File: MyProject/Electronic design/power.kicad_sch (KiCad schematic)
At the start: 7 parts

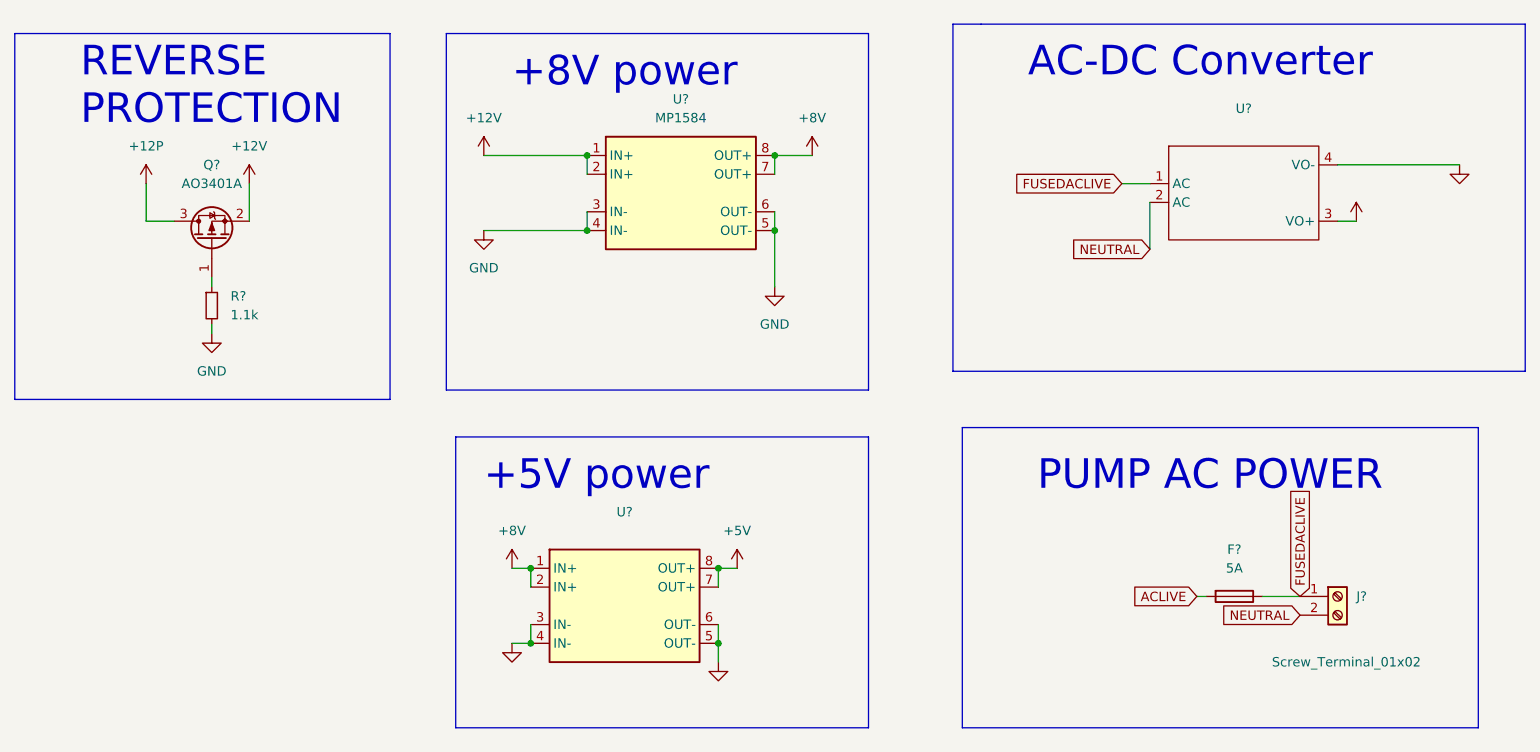
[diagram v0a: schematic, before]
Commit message: Shortening file names for Windows users
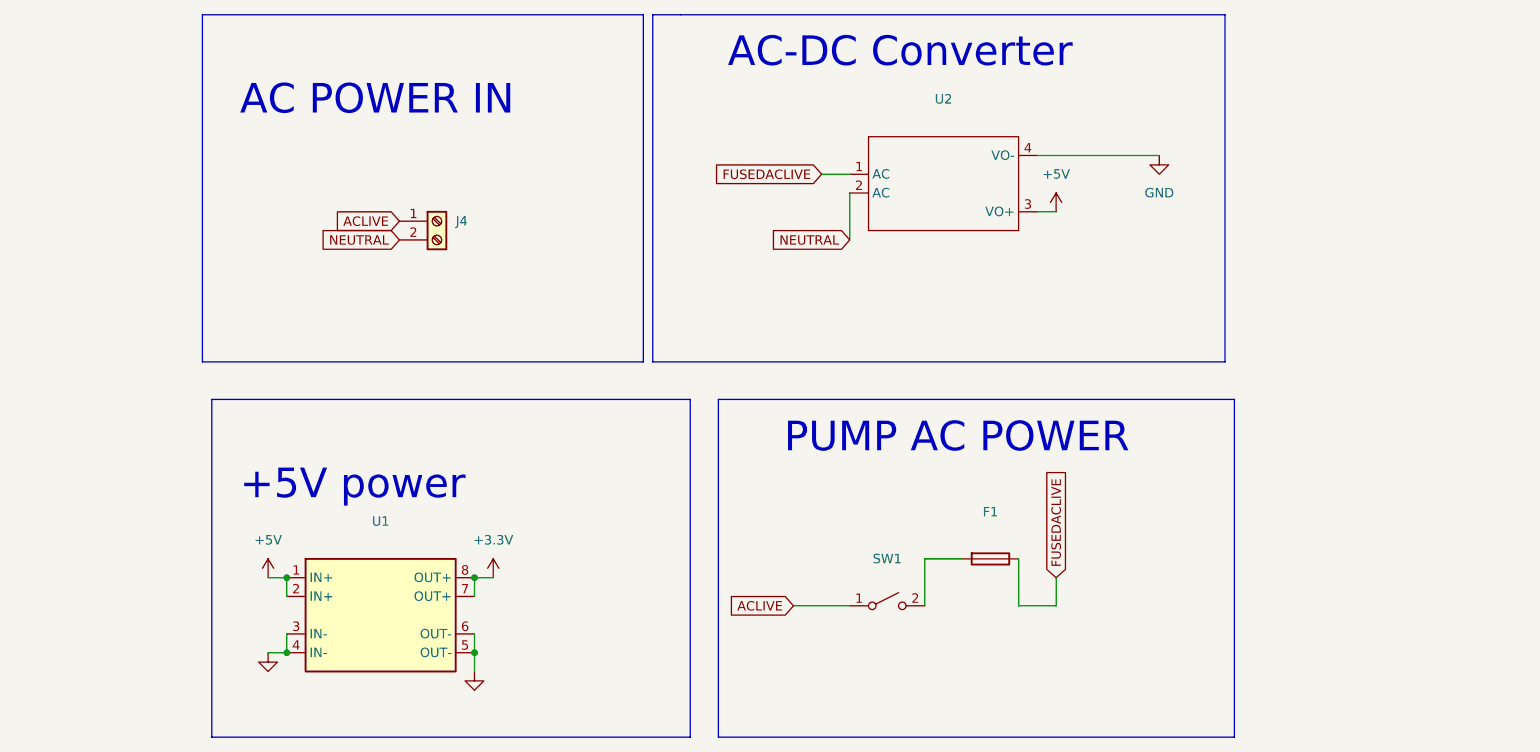
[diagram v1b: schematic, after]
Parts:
- removed J?: Screw_Terminal_01x02, symbol Connector:Screw_Terminal_01x02
- removed Q?: AO3401A, Package_TO_SOT_SMD:SOT-23, symbol Transistor_FET:AO3401A
- removed R?: 1.1k, Resistor_SMD:R_2010_5025Metric, symbol Device:R_Small
- removed U?: MP1584, Package_SO:SOIC-8-1EP_3.9x4.9mm_P1.27mm_EP2.29x3mm, symbol Userlibrary:MP1584
- added J4: (no value), symbol Connector:Screw_Terminal_01x02
- added SW1: (no value), symbol Switch:SW_SPST
- F1: renamed from F?; value 5A -> (none)
- U1: renamed from U?; value ~ -> (none)
- gave numbers to parts that had none: 1
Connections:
- net +8V is gone; now on net +5V: U1.1 (IN+), U1.2 (IN+)
- net +5V: no longer U1.7 (OUT+), U1.8 (OUT+)
- net ACLIVE: now also J4.1 (Pin_1), SW1.1 (A); no longer F1.2
- net NEUTRAL: now also J4.2 (Pin_2)
- new net: F1.2, SW1.2 (B)
- new net +3V3: U1.7 (OUT+), U1.8 (OUT+)
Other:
- note added: "AC POWER IN"
- note removed: "+8V power"
- note removed: "REVERSE PROTECTION"
- moved on the sheet: F1, U1, U2
